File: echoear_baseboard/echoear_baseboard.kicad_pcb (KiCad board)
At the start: 2 copper layers, 37.3 x 30.3 mm, 61 parts, among them Q1 AO3401A, Q2 AO3401A, SW1 TS-1088-AR02016, SW2 TS-1088-AR02016, SW3 TS-1088-AR02016, U1 TYPE-C 16PIN 2MD(073), U2 YZ92015035T-04025-01, U3 MountingHole_Pad, U4 A-SP1102DR6GHC-C01-2C, U5 MountingHole_Pad, U6 TLV62569DBV, U7 TP4057, U8 SAM8108

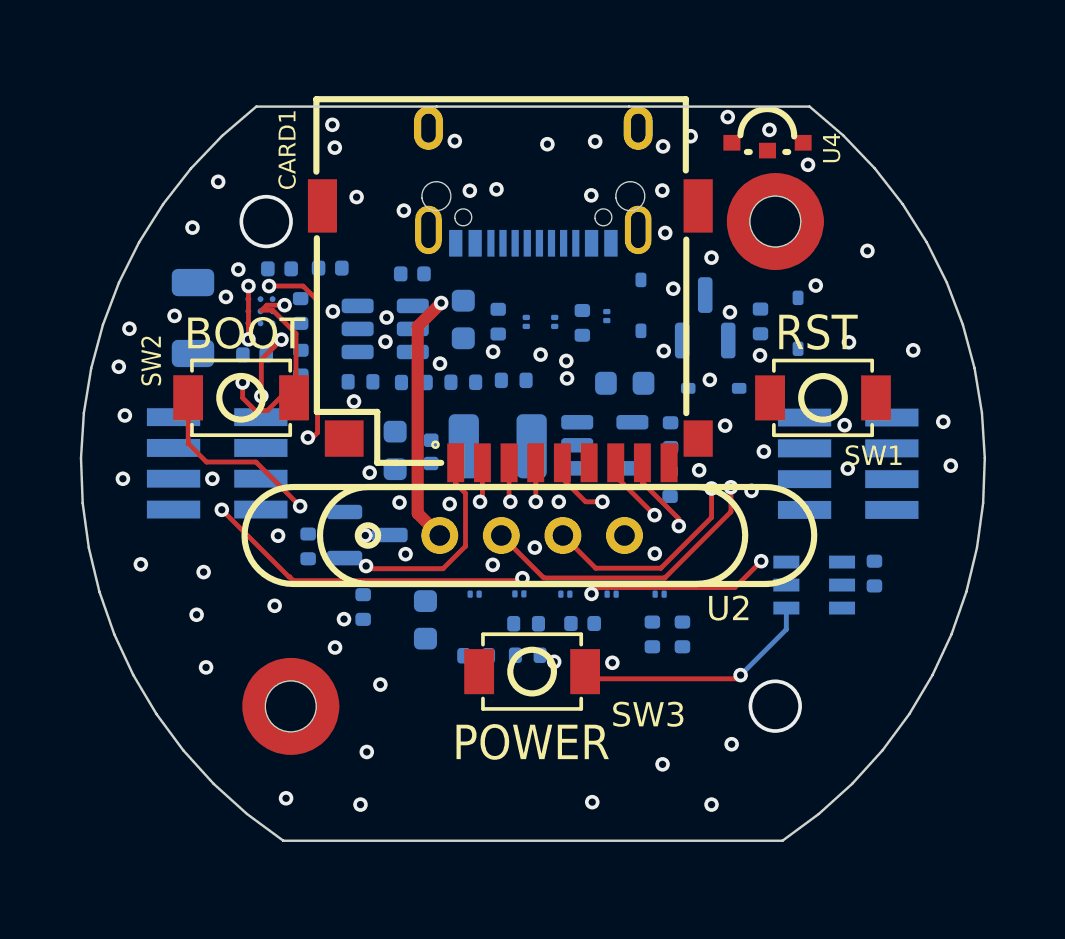
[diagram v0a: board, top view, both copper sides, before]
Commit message: Updated front traces & started back traces
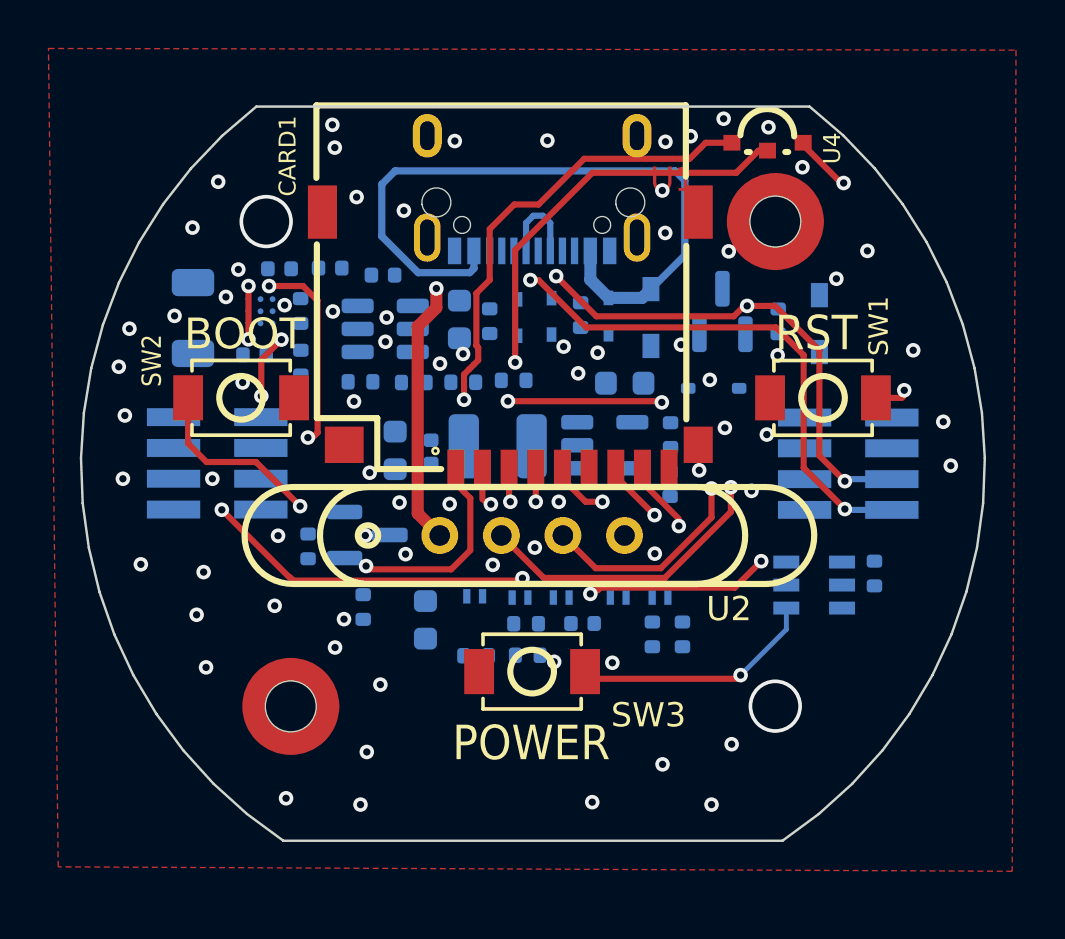
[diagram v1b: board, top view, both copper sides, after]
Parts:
- D1, D10: footprint Diode_SMD:D_SOD-323 -> Library:SOD-323_L1.8-W1.3-LS2.5-RD
- D2, D3, D4: footprint Diode_SMD:Infineon_SG-WLL-2-3_0.58x0.28_P0.36mm -> Library:SOD-523_L1.2-W0.8-LS1.6-BI
- D5, D6, D7, D8, D9: footprint Diode_SMD:Infineon_SG-WLL-2-3_0.58x0.28_P0.36mm -> Library:SOD-882_L1.0-W0.6-BI
- moved C9 1.21 mm to (107.7, 65.0)
- moved D10 0.88 mm to (125.7, 67.0)
- moved Q1 0.76 mm to (121.7, 66.5)
- moved R12 0.73 mm to (124.0, 66.9)
- moved D1 0.65 mm to (118.7, 66.7)
- moved D4 0.40 mm to (113.2, 66.7)
- moved R7 0.35 mm to (112.0, 66.8)
- moved R8 0.33 mm to (115.8, 66.6)
- moved U1 0.32 mm to (113.8, 61.6)
- moved D5 0.30 mm to (117.3, 78.2)
- moved D3 0.26 mm to (114.6, 66.7)
- moved CARD1 0.26 mm to (112.9, 67.7)
- moved D6 0.22 mm to (115.0, 78.2)
- moved C7 0.16 mm to (110.8, 66.8)
- moved D8 0.15 mm to (113.3, 78.2)
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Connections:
- U1 pad A7: /USD_DN -> /USB_DN
- U1 pad B6: Net-(D3-A1) -> /USB_DP
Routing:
- net /VBUS_IN: track 0.00 -> 29.5 mm, vias 2 -> 0
- net /USB_DP: track 0.00 -> 25.1 mm, vias 0 -> 2
- net /USB_DN: track 0.00 -> 20.1 mm, vias 0 -> 3
- net Net-(R10-Pad2): track 0.00 -> 19.0 mm, vias 0 -> 1
- net Net-(R9-Pad2): track 0.00 -> 16.7 mm, vias 0 -> 1
- net GND: track 8.37 -> 0.00 mm, vias 42 -> 54
- net /MCU_3V3: track 0.00 -> 6.37 mm, vias 2 -> 4
- net /VBUS: track 10.4 -> 13.3 mm, vias 1 -> 2
- net /ESP_RST: track 0.00 -> 1.42 mm, vias 0 -> 1
- net /VBAT: vias 1 -> 2
- net /USD_DN: vias 1 -> 0
- net (no net): vias 36 -> 17
- added copper zone on F.Cu, net GND

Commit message: Updated baseboard routing for BQ27220YZFR mainly
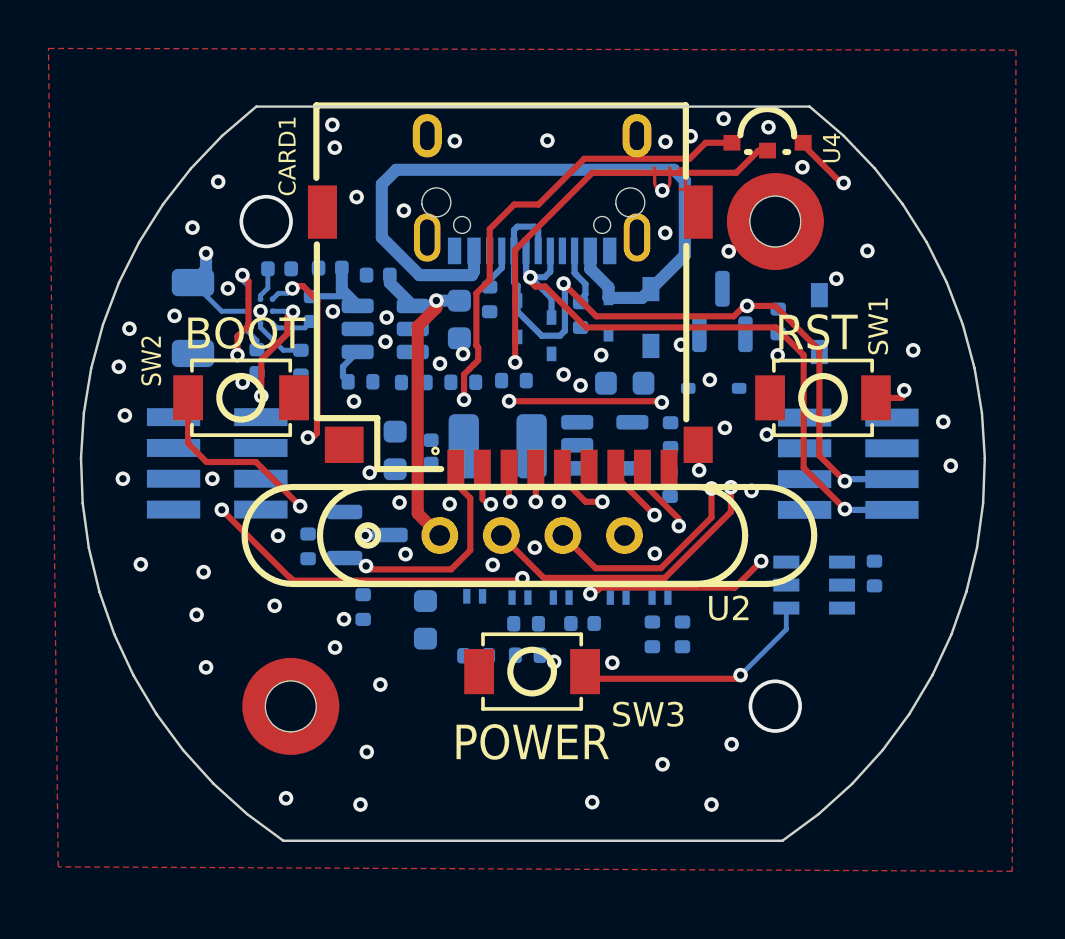
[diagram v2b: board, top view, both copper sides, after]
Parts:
- moved R7 0.90 mm to (112.0, 66.0)
- moved D3 0.80 mm to (114.6, 67.5)
- moved R17 0.46 mm to (104.7, 66.3)
- moved C12 0.28 mm to (102.5, 68.5), turned to -90 degrees
- moved C9 0.20 mm to (107.5, 65.0)
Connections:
- D3 pad 1: Net-(D3-A1) -> /USB_DP
- D4 pad 1: Net-(D4-A1) -> /USB_DN
- U1 pad B7: Net-(D4-A1) -> /USB_DN
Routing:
- net /USB_DN: track 20.1 -> 29.7 mm
- net /VBAT: track 0.00 -> 8.11 mm
- net /VBUS: track 13.3 -> 16.5 mm
- net /VBAT_IN: track 2.20 -> 4.70 mm
- net Net-(U1-CC2): track 0.00 -> 2.41 mm
- net /BAT_SDA: track 2.67 -> 4.90 mm
- net Net-(U9-BIN): track 0.00 -> 2.22 mm
- net Net-(U9-GPOUT): track 0.00 -> 1.79 mm
- net /CHRG: track 0.00 -> 1.57 mm
- net /USB_DP: track 25.1 -> 26.7 mm
- net Net-(U1-CC1): track 0.00 -> 1.55 mm
- net Net-(U9-VDD): track 0.00 -> 1.38 mm
- net Net-(U9-SRP): track 0.00 -> 1.23 mm

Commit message: Finishing routing of baseboard
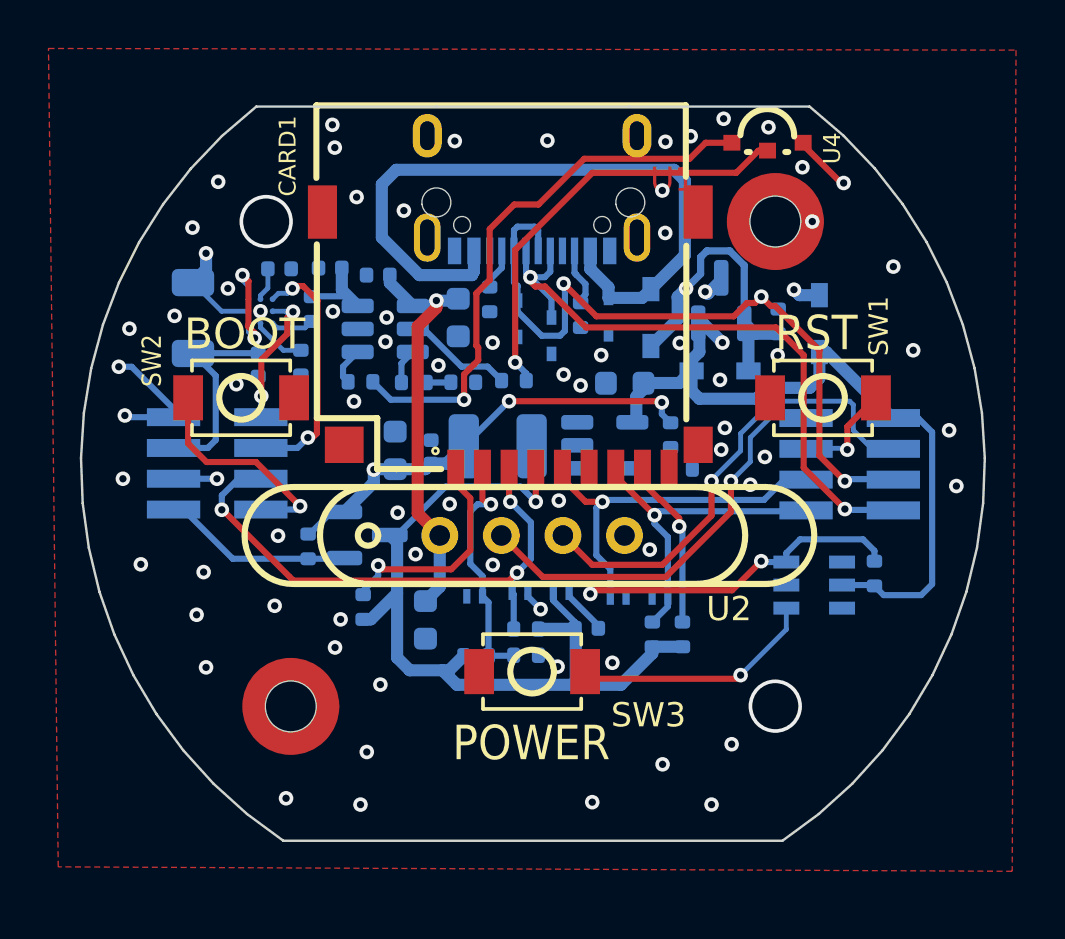
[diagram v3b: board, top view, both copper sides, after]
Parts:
- D11: footprint Diode_SMD:D_SOD-323 -> Library:SOD-323_L1.8-W1.3-LS2.5-RD
- moved D11 0.77 mm to (121.5, 68.9)
- moved R14 0.74 mm to (119.9, 73.0), turned to 0 degrees
- moved G*** 0.53 mm to (104.9, 85.8)
- moved Q1 0.45 mm to (121.6, 66.0)
- moved C2 0.26 mm to (116.0, 79.5)
- moved R3 0.22 mm to (113.5, 79.5)
- moved D6 0.20 mm to (115.0, 78.0)
- moved D8 0.20 mm to (113.3, 78.0)
- moved C12 0.16 mm to (102.5, 68.7)
- moved C7 0.09 mm to (110.8, 66.7)
- moved R1 0.07 mm to (113.5, 80.6)
- moved H2 0.06 mm to (126.9, 72.8)
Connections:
- C12 pad 1: Net-(U9-SRP) -> /VBAT_IN
- Q2 pad 1: Net-(CARD1-DAT2) -> /POWER_CTRL
- R19 pad 1: Net-(U9-SRP) -> /VBAT_IN
- U9 pad C1: Net-(U9-SRP) -> /VBAT_IN
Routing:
- net /VCC_3V3: track 1.61 -> 35.7 mm, vias 2 -> 1
- net /VIN: track 0.00 -> 31.0 mm, vias 0 -> 2
- net /VBUS: track 16.5 -> 32.1 mm, vias 2 -> 3
- net /MCU_3V3: track 6.32 -> 20.0 mm
- net /SD_CLK: track 2.70 -> 15.7 mm
- net /SD_DA0: track 2.82 -> 14.0 mm
- net /U1TXD: track 8.75 -> 19.3 mm
- net GND: track 0.00 -> 9.22 mm, vias 54 -> 64
- net /VBAT_IN: track 4.70 -> 13.7 mm
- net Net-(CARD1-CD/DAT3): track 1.94 -> 10.3 mm
- net /SD_CMD: track 15.3 -> 23.5 mm
- net /POWER_CTRL: track 0.00 -> 7.90 mm
- net /PWR_EN: track 7.61 -> 13.5 mm
- net /U1RXD: track 12.3 -> 17.0 mm
- net /STDBY: track 0.00 -> 4.54 mm
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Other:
- board text added: "gndZones"

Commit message: Finished baseboard routing v1
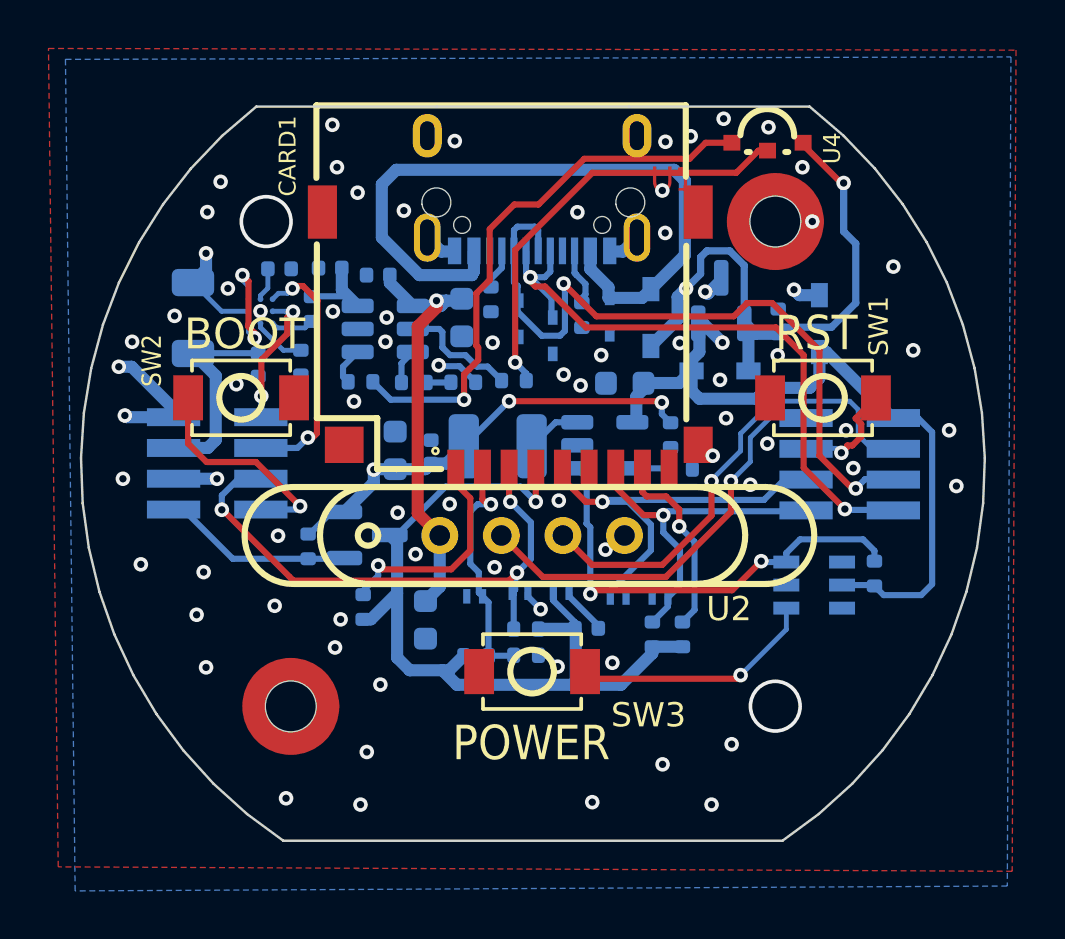
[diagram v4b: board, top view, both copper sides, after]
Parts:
- moved C7 0.15 mm to (110.9, 66.7)
- moved D3 0.05 mm to (114.7, 67.5)
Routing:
- net /VBUS: track 32.1 -> 41.4 mm
- net /PWR_EN: track 13.5 -> 19.3 mm
- net GND: track 9.22 -> 14.8 mm, vias 64 -> 73
- net Net-(U6-FB): track 0.00 -> 2.41 mm
- net Net-(U6-SW): track 0.00 -> 2.29 mm
- net /SD_CLK: track 15.7 -> 17.5 mm
- net Net-(CARD1-DAT1): track 7.27 -> 8.13 mm
- net /USB_DN: vias 3 -> 2
- net /VIN: vias 2 -> 1
- net (no net): vias 6 -> 0
- added copper zone on B.Cu, net GND
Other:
- board text removed: "gndZones"
